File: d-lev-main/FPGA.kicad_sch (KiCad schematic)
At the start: 14 parts, among them J2 Tag-Connect TC2030-NL, U1 25LCxxx, U3 AC608

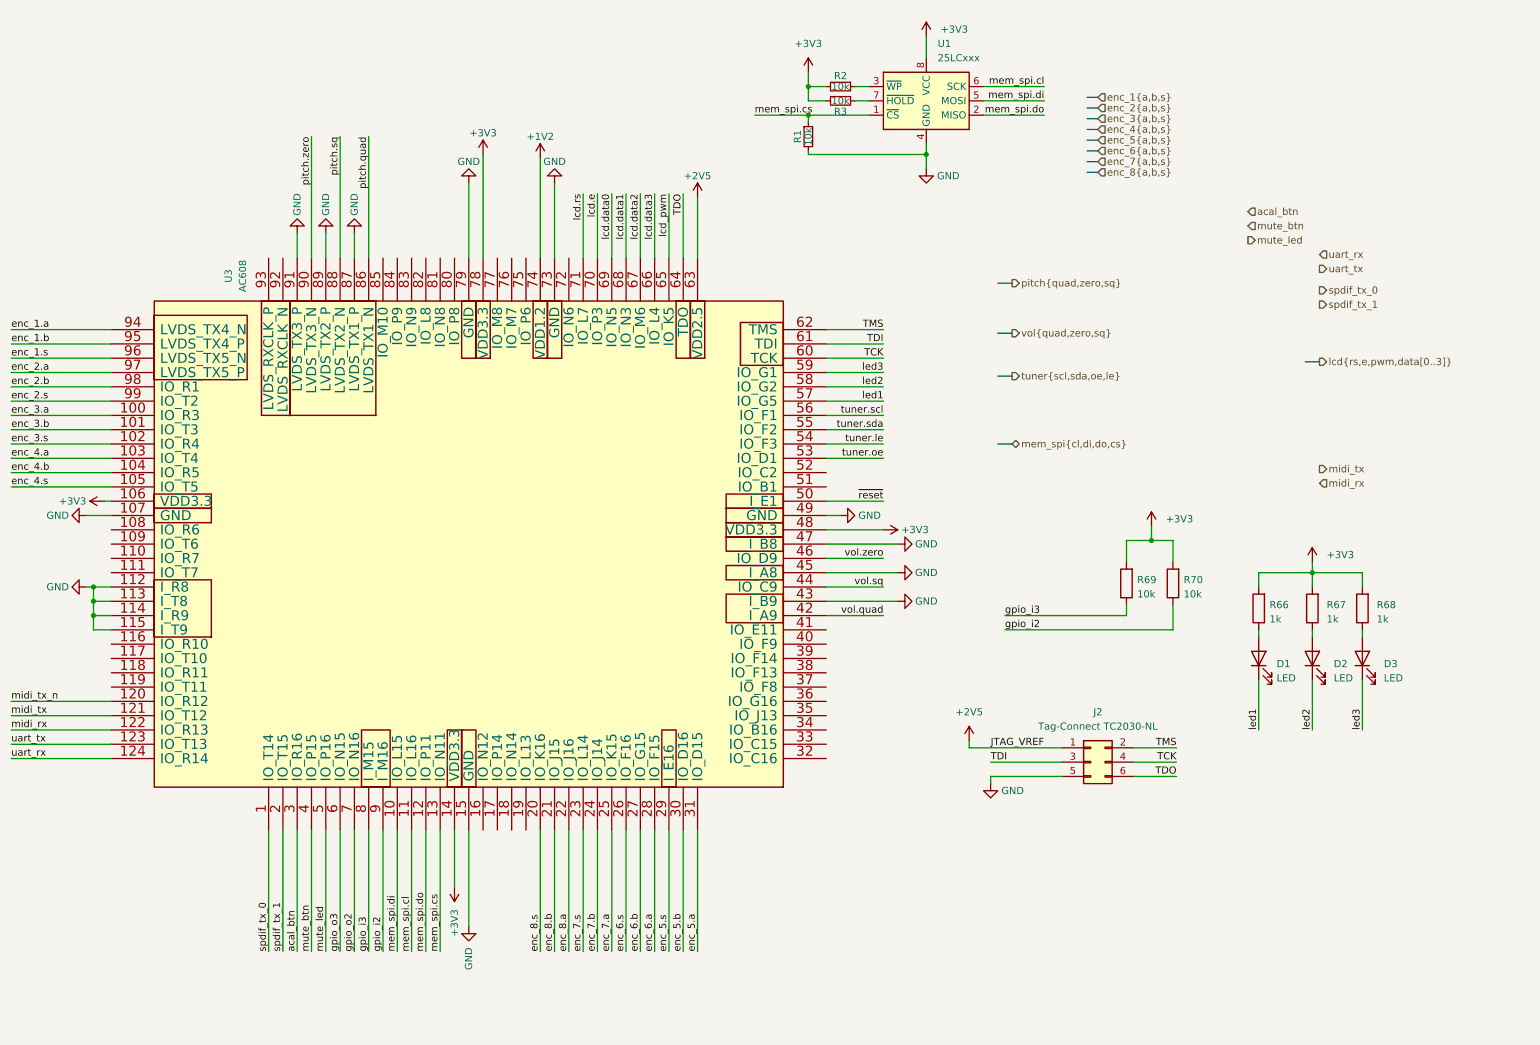
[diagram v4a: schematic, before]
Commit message: mostly done routing
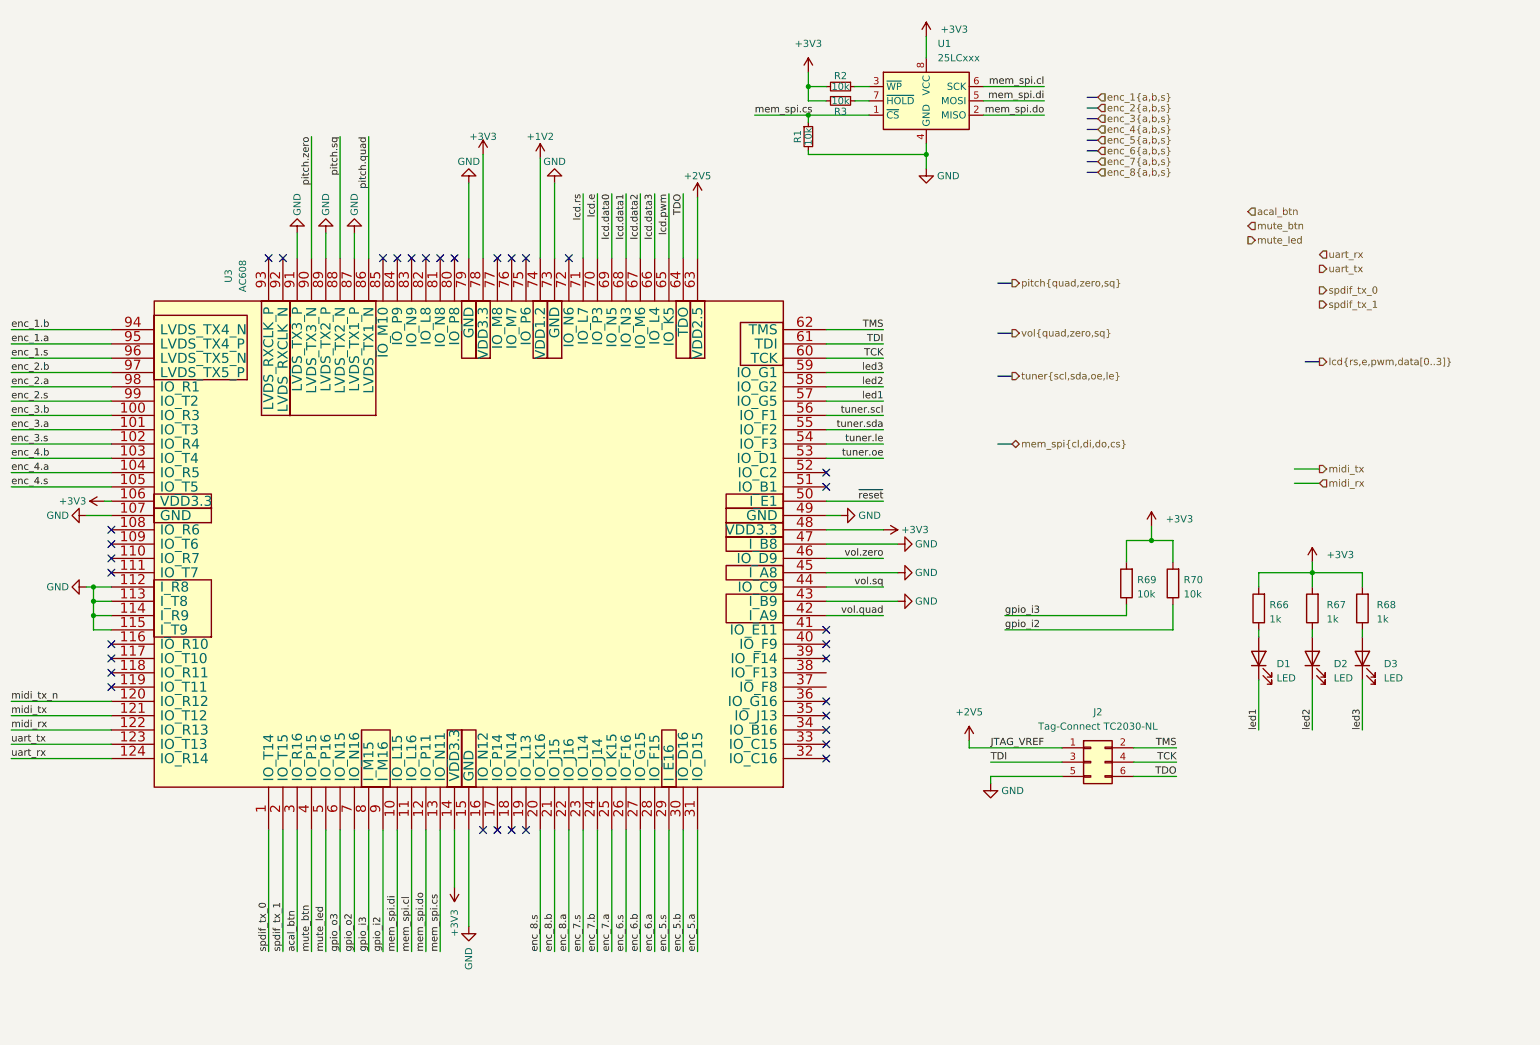
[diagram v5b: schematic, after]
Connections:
- net enc_1.a: now also U3.95 (LVDS_TX4_P); no longer U3.94 (LVDS_TX4_N)
- net enc_1.b: now also U3.94 (LVDS_TX4_N); no longer U3.95 (LVDS_TX4_P)
- net enc_2.a: now also U3.98 (IO_R1); no longer U3.97 (LVDS_TX5_P)
- net enc_2.b: now also U3.97 (LVDS_TX5_P); no longer U3.98 (IO_R1)
- net enc_3.a: now also U3.101 (IO_T3); no longer U3.100 (IO_R3)
- net enc_3.b: now also U3.100 (IO_R3); no longer U3.101 (IO_T3)
- net enc_4.a: now also U3.104 (IO_R5); no longer U3.103 (IO_T4)
- net enc_4.b: now also U3.103 (IO_T4); no longer U3.104 (IO_R5)
- net lcd_pwm renamed lcd.pwm
- no-connect marks 0 -> 34
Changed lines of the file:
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@@
   (junction (at 181.61 40.64) (diameter 0) (color 0 0 0 0)
   )
+  (no_connect (at 87.63 59.055))
+  (no_connect (at 85.09 59.055))
+  (no_connect (at 67.31 59.055))
+  (no_connect (at 163.83 99.695))
+  (no_connect (at 163.83 97.155))
+  (no_connect (at 110.49 59.055))
+  (no_connect (at 163.83 137.795))
+  (no_connect (at 105.41 160.655))
+  (no_connect (at 107.95 160.655))
+  (no_connect (at 36.83 135.255))
+  (no_connect (at 97.79 59.055))
+  (no_connect (at 36.83 112.395))
+  (no_connect (at 163.83 130.175))
+  (no_connect (at 110.49 160.655))
+  (no_connect (at 92.71 59.055))
+  (no_connect (at 90.17 59.055))
+  (no_connect (at 118.11 59.055))
+  (no_connect (at 107.95 59.055))
+  (no_connect (at 163.83 147.955))
+  (no_connect (at 36.83 132.715))
+  (no_connect (at 64.77 59.055))
+  (no_connect (at 163.83 142.875))
+  (no_connect (at 36.83 109.855))
+  (no_connect (at 36.83 107.315))
+  (no_connect (at 105.41 59.055))
+  (no_connect (at 163.83 140.335))
+  (no_connect (at 36.83 127.635))
+  (no_connect (at 163.83 125.095))
+  (no_connect (at 163.83 145.415))
+  (no_connect (at 36.83 114.935))
+  (no_connect (at 95.25 59.055))
+  (no_connect (at 36.83 130.175))
+  (no_connect (at 163.83 127.635))
+  (no_connect (at 102.87 160.655))
   (wire (pts (xy 19.05 84.455) (xy 36.83 84.455))
     (stroke (width 0) (type default))
@@
     (stroke (width 0) (type default))
   )
+  (wire (pts (xy 247.015 99.06) (xy 251.46 99.06))
+    (stroke (width 0) (type default))
+  )
   (bus (pts (xy 210.185 38.1) (xy 212.09 38.1))
     (stroke (width 0) (type default))
@@
     (stroke (width 0) (type default))
   )
+  (wire (pts (xy 247.015 96.52) (xy 251.46 96.52))
+    (stroke (width 0) (type default))
+  )
   (wire (pts (xy 163.83 112.395) (xy 173.99 112.395))
     (stroke (width 0) (type default))
@@
     (effects (font (size 1.27 1.27)) (justify left bottom))
   )
-  (label "enc_3.a" (at 19.05 86.995 0) (fields_autoplaced)
+  (label "enc_3.a" (at 19.05 89.535 0) (fields_autoplaced)
     (effects (font (size 1.27 1.27)) (justify left bottom))
   )
@@
     (effects (font (size 1.27 1.27)) (justify left bottom))
   )
-  (label "enc_4.b" (at 19.05 97.155 0) (fields_autoplaced)
-    (effects (font (size 1.27 1.27)) (justify left bottom))
-  )
-  (label "enc_3.b" (at 19.05 89.535 0) (fields_autoplaced)
+  (label "enc_4.b" (at 19.05 94.615 0) (fields_autoplaced)
+    (effects (font (size 1.27 1.27)) (justify left bottom))
+  )
+  (label "enc_3.b" (at 19.05 86.995 0) (fields_autoplaced)
     (effects (font (size 1.27 1.27)) (justify left bottom))
   )
@@
     (effects (font (size 1.27 1.27)) (justify right bottom))
   )
-  (label "enc_2.b" (at 19.05 81.915 0) (fields_autoplaced)
+  (label "enc_2.b" (at 19.05 79.375 0) (fields_autoplaced)
     (effects (font (size 1.27 1.27)) (justify left bottom))
   )
@@
     (effects (font (size 1.27 1.27)) (justify left bottom))
   )
-  (label "lcd_pwm" (at 135.89 47.625 270) (fields_autoplaced)
+  (label "lcd.pwm" (at 135.89 47.625 270) (fields_autoplaced)
     (effects (font (size 1.27 1.27)) (justify right bottom))
   )
@@
     (effects (font (size 1.27 1.27)) (justify right bottom))
   )
-  (label "enc_1.b" (at 19.05 74.295 0) (fields_autoplaced)
+  (label "enc_1.b" (at 19.05 71.755 0) (fields_autoplaced)
     (effects (font (size 1.27 1.27)) (justify left bottom))
   )
@@
     (effects (font (size 1.27 1.27)) (justify left bottom))
   )
-  (label "enc_2.a" (at 19.05 79.375 0) (fields_autoplaced)
+  (label "enc_2.a" (at 19.05 81.915 0) (fields_autoplaced)
     (effects (font (size 1.27 1.27)) (justify left bottom))
   )
@@
     (effects (font (size 1.27 1.27)) (justify left bottom))
   )
-  (label "enc_1.a" (at 19.05 71.755 0) (fields_autoplaced)
+  (label "enc_1.a" (at 19.05 74.295 0) (fields_autoplaced)
     (effects (font (size 1.27 1.27)) (justify left bottom))
   )
@@
     (effects (font (size 1.27 1.27)) (justify left bottom))
   )
-  (label "enc_4.a" (at 19.05 94.615 0) (fields_autoplaced)
+  (label "enc_4.a" (at 19.05 97.155 0) (fields_autoplaced)
     (effects (font (size 1.27 1.27)) (justify left bottom))
   )
@@
     )
   )
-  (symbol (lib_id "power:+1V2") (at 113.03 41.275 0) (unit 1)
+  (symbol (lib_name "+3V3_1") (lib_id "power:+3V3") (at 102.87 40.64 0) (unit 1)
     (in_bom yes) (on_board yes) (dnp no) (fields_autoplaced)
-    (property "Reference" "#PWR015" (at 113.03 45.085 0)
-      (effects (font (size 1.27 1.27)) hide)
-    )
-    (property "Value" "+1V2" (at 113.03 37.465 0)
-      (effects (font (size 1.27 1.27)))
-    )
-    (property "Footprint" "" (at 113.03 41.275 0)
-      (effects (font (size 1.27 1.27)) hide)
-    )
-    (property "Datasheet" "" (at 113.03 41.275 0)
+    (property "Reference" "#PWR015" (at 102.87 44.45 0)
+      (effects (font (size 1.27 1.27)) hide)
+    )
+    (property "Value" "+3V3" (at 102.87 37.465 0)
+      (effects (font (size 1.27 1.27)))
+    )
+    (property "Footprint" "" (at 102.87 40.64 0)
+      (effects (font (size 1.27 1.27)) hide)
+    )
+    (property "Datasheet" "" (at 102.87 40.64 0)
       (effects (font (size 1.27 1.27)) hide)
     )
@@
     )
   )
-  (symbol (lib_id "power:+3V3") (at 102.87 40.64 0) (unit 1)
+  (symbol (lib_name "+1V2_1") (lib_id "power:+1V2") (at 113.03 41.275 0) (unit 1)
     (in_bom yes) (on_board yes) (dnp no) (fields_autoplaced)
-    (property "Reference" "#PWR016" (at 102.87 44.45 0)
-      (effects (font (size 1.27 1.27)) hide)
-    )
-    (property "Value" "+3V3" (at 102.87 36.83 0)
-      (effects (font (size 1.27 1.27)))
-    )
-    (property "Footprint" "" (at 102.87 40.64 0)
-      (effects (font (size 1.27 1.27)) hide)
-    )
-    (property "Datasheet" "" (at 102.87 40.64 0)
-      (effects (font (size 1.27 1.27)) hide)
-    )
-    (pin "1")
-    (instances
-      (project "dlev-mini"
-        (path "/eb5e8bfd-9871-4528-bf57-58851bf63907/acdfb54c-8449-4fbe-9778-47a925c872ef"
-          (reference "#PWR016") (unit 1)
-        )
-      )
+    (property "Reference" "#PWR099" (at 113.03 45.085 0)
+      (effects (font (size 1.27 1.27)) hide)
+    )
+    (property "Value" "+1V2" (at 113.03 37.465 0)
+      (effects (font (size 1.27 1.27)))
+    )
+    (property "Footprint" "" (at 113.03 41.275 0)
+      (effects (font (size 1.27 1.27)) hide)
+    )
+    (property "Datasheet" "" (at 113.03 41.275 0)
+      (effects (font (size 1.27 1.27)) hide)
+    )
+    (pin "1")
+    (instances
+      (project "dlev-mini"
+        (path "/eb5e8bfd-9871-4528-bf57-58851bf63907/acdfb54c-8449-4fbe-9778-47a925c872ef"
+          (reference "#PWR099") (unit 1)
+        )
+      )

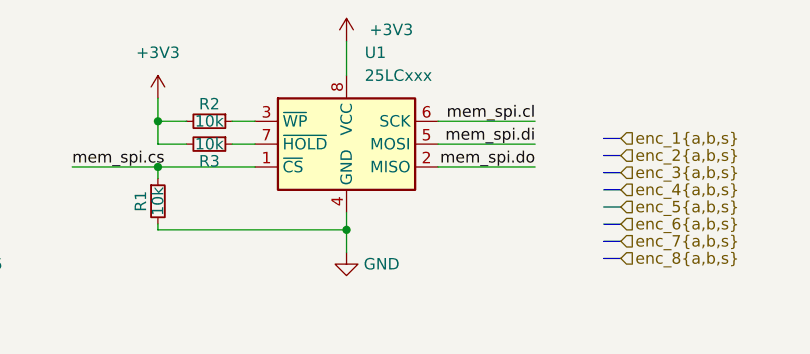
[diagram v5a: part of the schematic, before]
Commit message: Clean up unroutes and add DRC
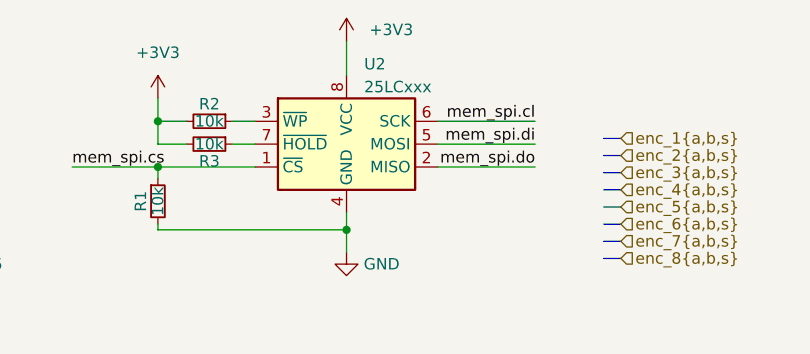
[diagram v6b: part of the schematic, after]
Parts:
- removed U1: 25LCxxx, Package_SO:SOIC-8W_5.3x5.3mm_P1.27mm, symbol Memory_EEPROM:25LCxxx
- added U2: 25LCxxx, Package_SO:SOIC-8_5.275x5.275mm_P1.27mm, symbol Memory_EEPROM:25LCxxx
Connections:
- net +3V3: now also U2.8 (VCC)
- net GND: now also U2.4 (GND)
- net mem_spi.cl: now also U2.6 (SCK)
- net mem_spi.cs: now also U2.1 (~{CS})
- net mem_spi.di: now also U2.5 (MOSI)
- net mem_spi.do: now also U2.2 (MISO)
- net at R2.1: now also U2.3 (~{WP})
- net at R3.1: now also U2.7 (~{HOLD})

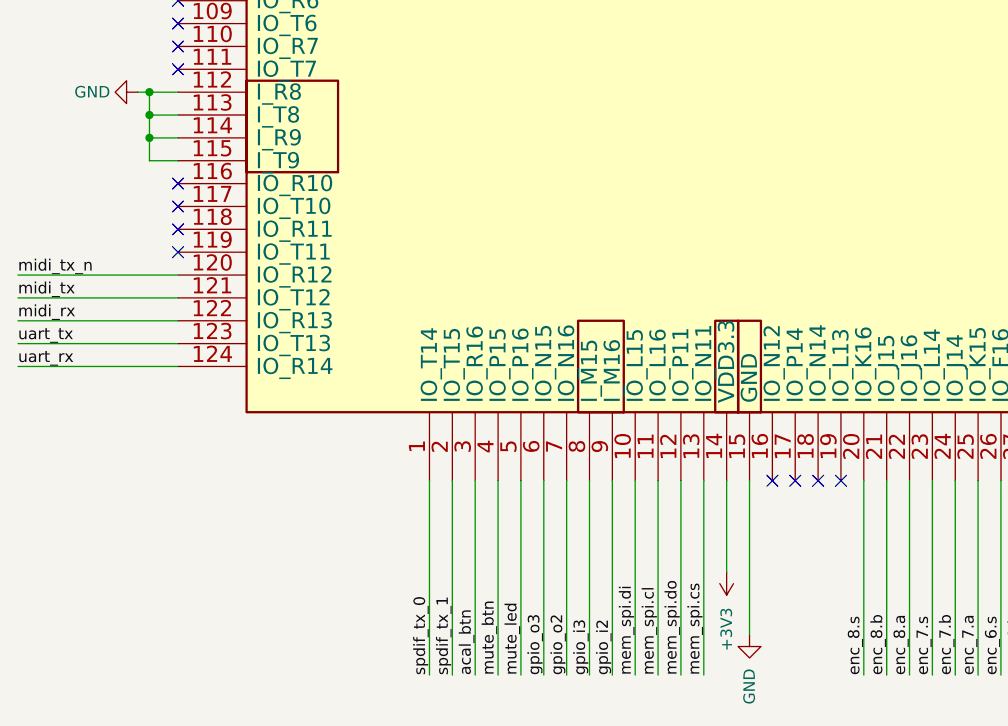
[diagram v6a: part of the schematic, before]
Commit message: Improve routing and rearrange I/O connector
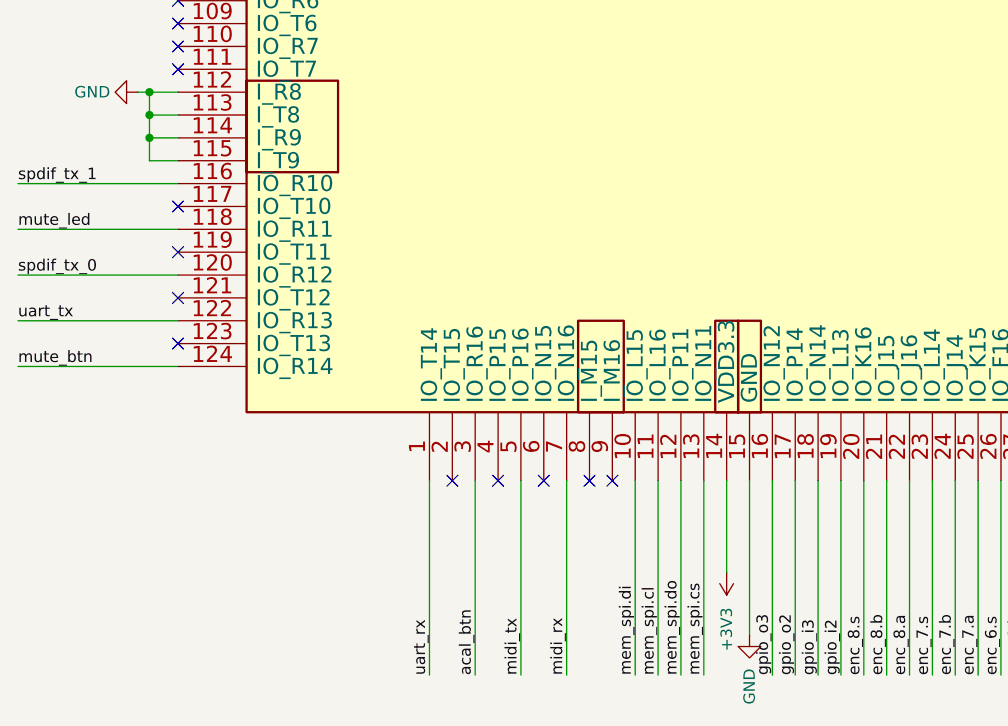
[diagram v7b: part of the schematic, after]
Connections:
- net midi_tx_n is gone; now on net spdif_tx_0: U3.120 (IO_R12)
- net gpio_i2: now also U3.19 (IO_L13); no longer U3.9 (I_M16)
- net gpio_i3: now also U3.18 (IO_N14); no longer U3.8 (I_M15)
- net gpio_o2: now also U3.17 (IO_P14); no longer U3.7 (IO_N16)
- net gpio_o3: now also U3.16 (IO_N12); no longer U3.6 (IO_N15)
- net midi_rx: now also U3.7 (IO_N16); no longer U3.122 (IO_R13)
- net midi_tx: now also U3.5 (IO_P16); no longer U3.121 (IO_T12)
- net mute_btn: now also U3.124 (IO_R14); no longer U3.4 (IO_P15)
- net mute_led: now also U3.118 (IO_R11); no longer U3.5 (IO_P16)
- net spdif_tx_0: no longer U3.1 (IO_T14)
- net spdif_tx_1: now also U3.116 (IO_R10); no longer U3.2 (IO_T15)
- net uart_rx: now also U3.1 (IO_T14); no longer U3.124 (IO_R14)
- net uart_tx: now also U3.122 (IO_R13); no longer U3.123 (IO_T13)
- no-connect marks 34 -> 35

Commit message: many many changes'
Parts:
- removed R69, R70: 10k, Resistor_SMD:R_0603_1608Metric, symbol Device:R
- added C22: .01u, Capacitor_SMD:C_0603_1608Metric, symbol Device:C_Small
- added R15: 10k, Resistor_SMD:R_0603_1608Metric, symbol Device:R
- added R16: 1k, Resistor_SMD:R_0603_1608Metric, symbol Device:R
- added SW10, SW9: SW_Push, Button_Switch_SMD:SW_SPST_B3U-1000P, symbol Switch:SW_Push
- added TP1: 2v5, TestPoint:TestPoint_Pad_D1.0mm, symbol Connector:TestPoint
- added TP2: 1v2, TestPoint:TestPoint_Pad_D1.0mm, symbol Connector:TestPoint
- added TP3: 3v3, TestPoint:TestPoint_Pad_D1.0mm, symbol Connector:TestPoint
- added TP4: GPIO_O3, TestPoint:TestPoint_Pad_D1.0mm, symbol Connector:TestPoint
- added TP5: GPIO_O2, TestPoint:TestPoint_Pad_D1.0mm, symbol Connector:TestPoint
- added TP6: GPIO_I3, TestPoint:TestPoint_Pad_D1.0mm, symbol Connector:TestPoint
- added TP7: GPIO_I2, TestPoint:TestPoint_Pad_D1.0mm, symbol Connector:TestPoint
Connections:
- net +2V5: now also TP1.1
- net +3V3: now also R15.2, TP3.1
- net GND: now also C22.2, R16.1, SW9.2
- net acal_btn: now also SW10.1
- net gpio_i2: now also TP7.1
- net gpio_i3: now also TP6.1
- net gpio_o2: now also TP5.1
- net gpio_o3: now also TP4.1
- net ~{reset}: now also C22.1, R15.1, SW9.1
- net +1V2: no longer names the net of U3.74 (VDD1.2)
- net +1V2: now also TP2.1
- new net: R16.2, SW10.2
